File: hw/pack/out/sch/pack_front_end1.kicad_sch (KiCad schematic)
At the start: 14 parts, among them J1 3.5mm locking, U3 OPA1656

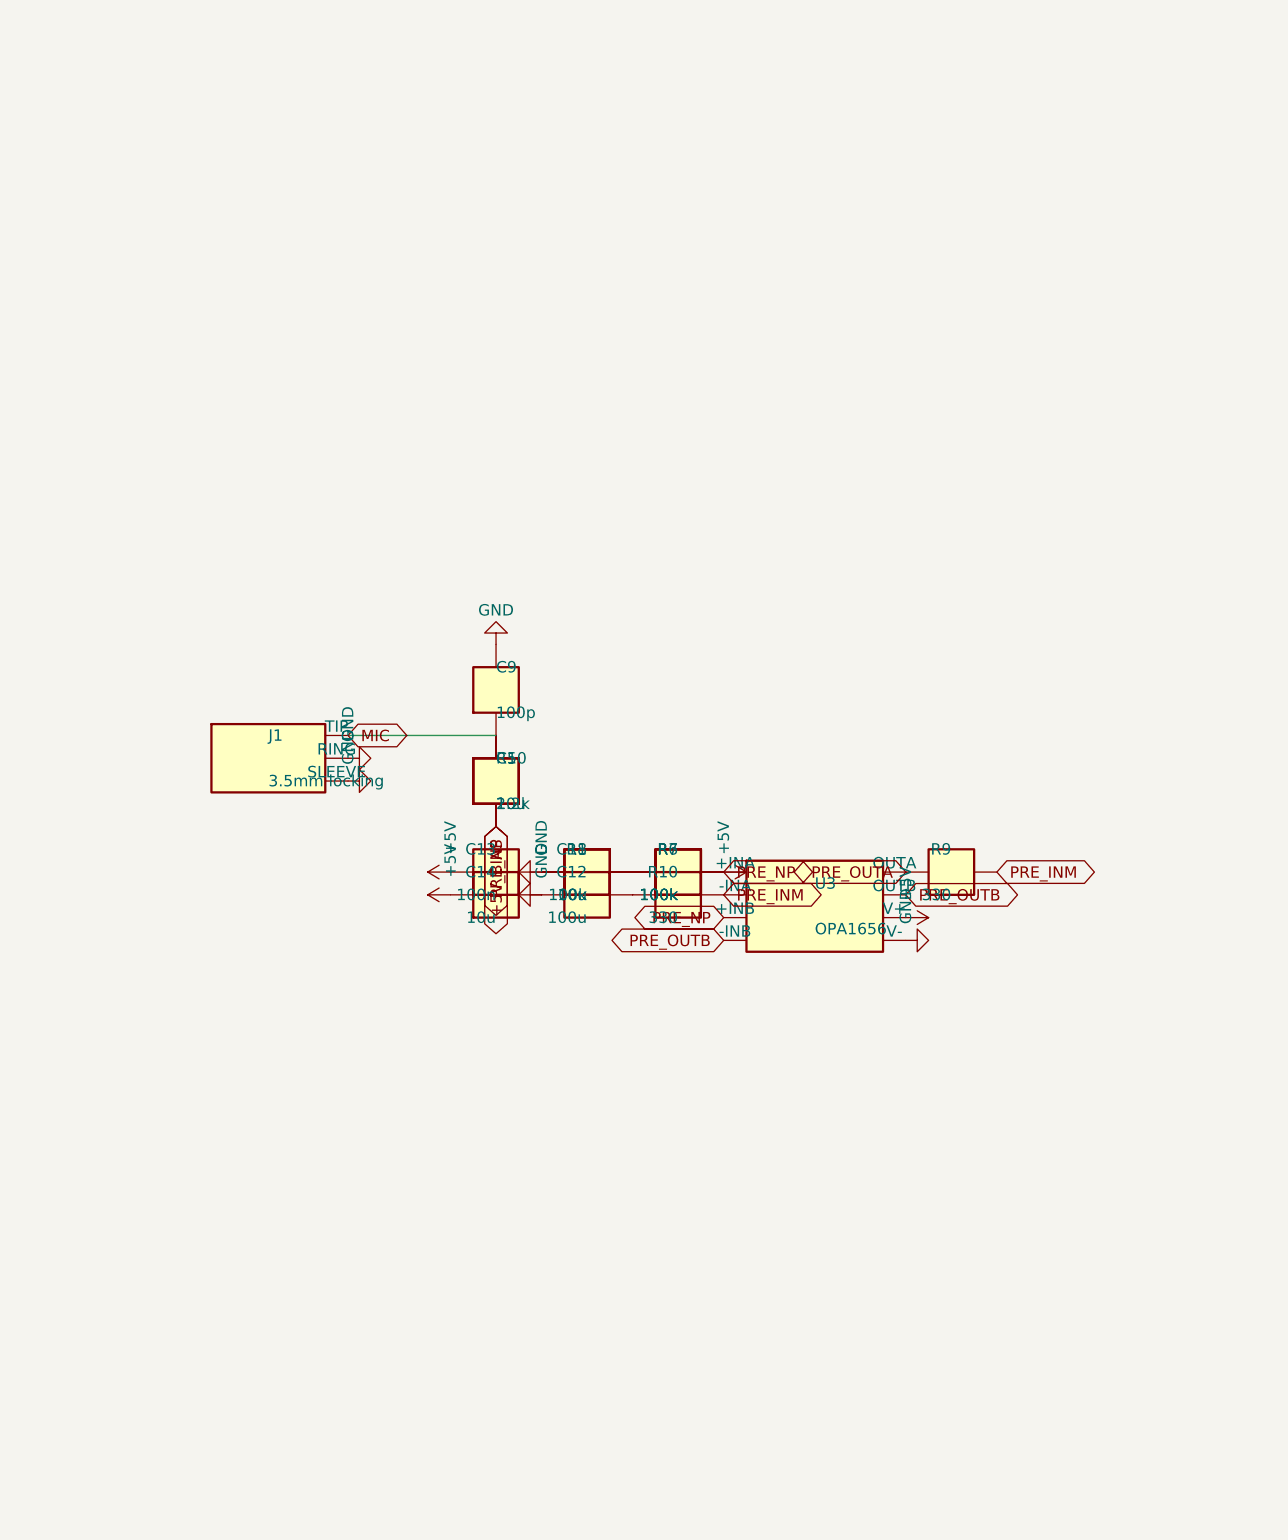
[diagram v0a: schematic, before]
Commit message: hw/pack: review fixes for #75 (op-amp CM, hot-plug protection, CI, cutoff, LEDs) (#31)
- VCM 180k/100k (1.77 V) keeps OPA1656 +IN inside V+ - 2.25 V; SPICE clamp 0.25/4.70 V,
  test asserts input CM, ADC pin (1.375 V) and prints numbers in CI (-rP)
- tip ESD (TPD1E10B06), BAV199 clamp + 100R ahead of the op-amp; C9 22p; noise 0.96 uV
- CI installs skidl==3.0.0, pack test fails (not skips) under CI, stale-output diff check
- no PTC; cell sensed at BAT+; firmware cutoff 3.2 V derived in audit.py; PK-8 LED
  thresholds -10/-7 dBFS; real LED MPNs; VDDH decoupling; audit prints DK-price BOM

Co-Authored-By: Claude Opus 5.5 <noreply@anthropic.com>
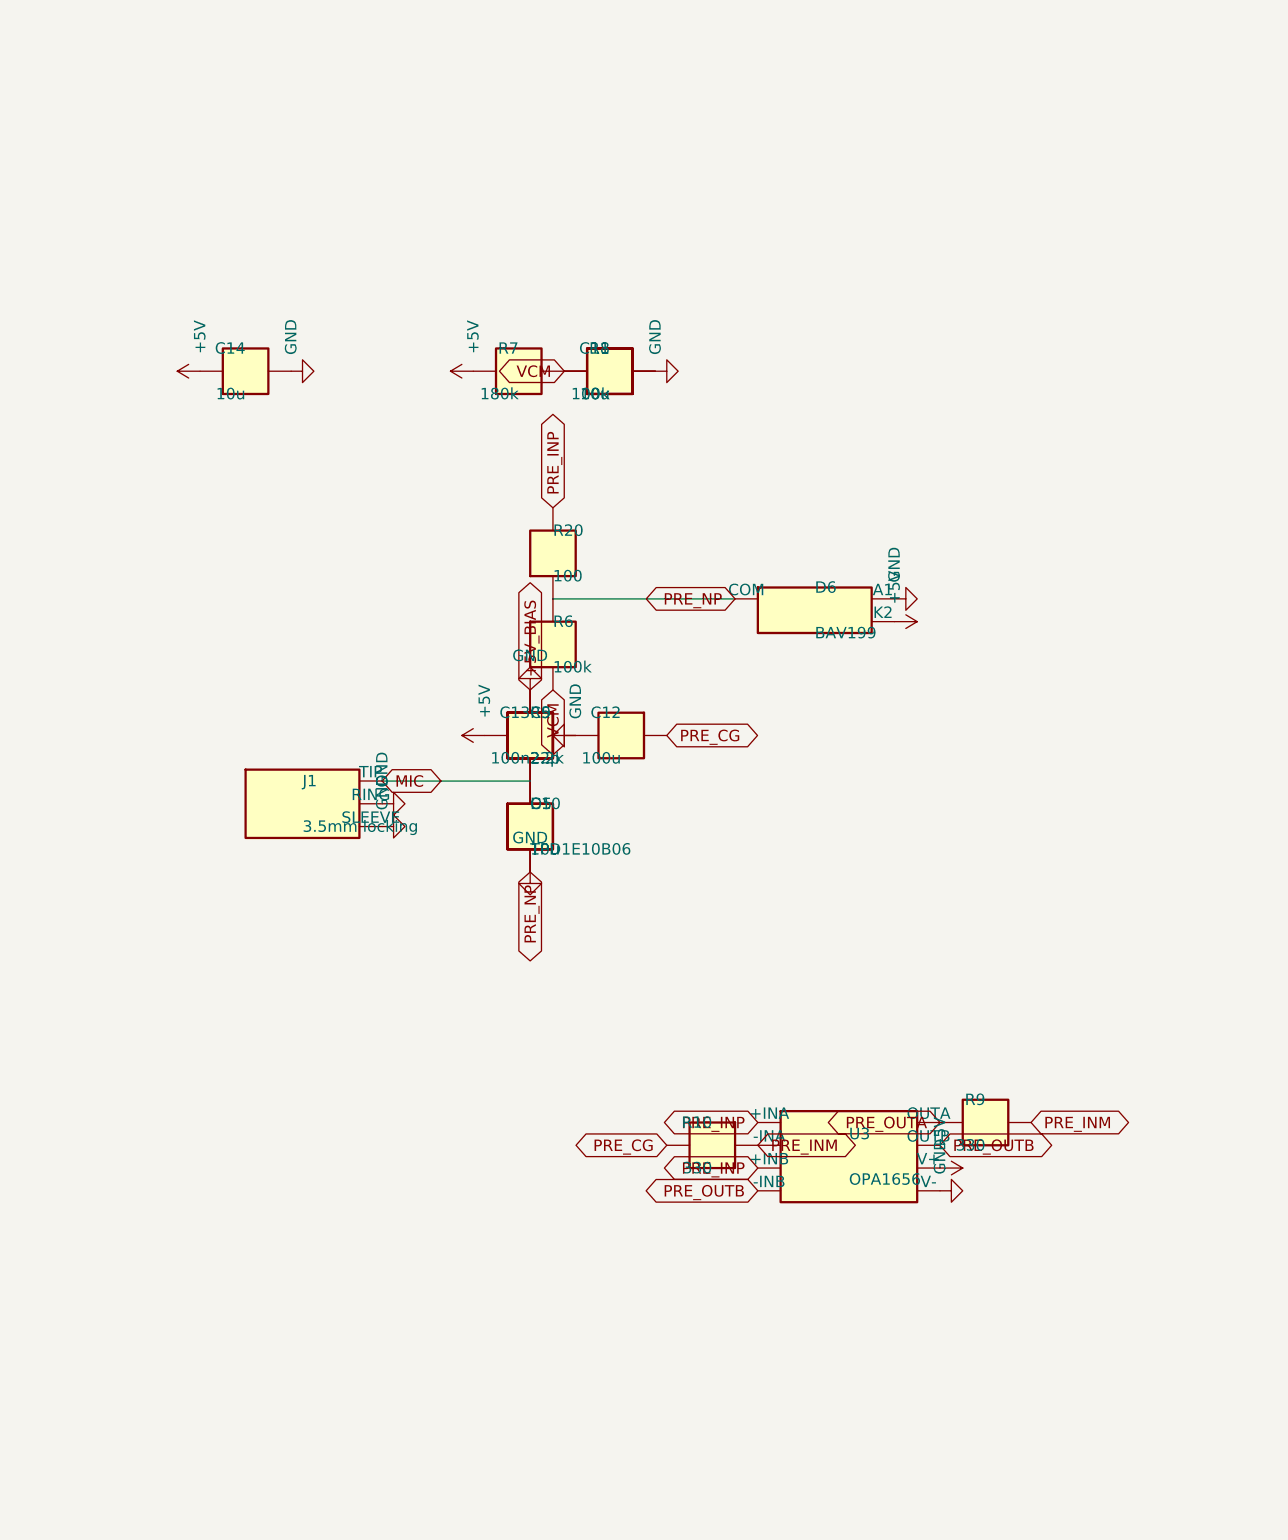
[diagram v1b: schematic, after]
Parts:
- added D5: TPD1E10B06, Diode_SMD:D_0402_1005Metric, symbol openpack:ESD_Bidir
- added D6: BAV199, Package_TO_SOT_SMD:SOT-23, symbol openpack:BAV199
- added R20: 100, Resistor_SMD:R_0402_1005Metric, symbol openpack:R
- C9: value 100p -> 22p; MPN C_100p_0402_C0G -> C_22p_0402_C0G
- R7: value 100k -> 180k
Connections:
- net +5V: now also D6.2 (K2); no longer C10.2, R5.1, R6.1, U3.3 (+INA), U3.5 (+INB)
- net GND: now also C10.2, R5.1, R6.1, D5.2, D6.1 (A1), D6.3 (COM), R20.1
- net MIC: now also D5.1
- net VCM: now reaches C11.1, R6.2, R7.2, R8.1
- net PRE_CG: now reaches C12.1, R10.2
- new net PRE_INP: R20.2, U3.3 (+INA), U3.5 (+INB)
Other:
- moved on the sheet: C10, C11, C12, C13, C14, C9, J1, R10, R5, R6, R7, R8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

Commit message: hw/pack: 3 A chip fuse (23 mOhm) on BAT+, cutoff re-derived, BOM $34.98 (#31)
Co-Authored-By: Claude Opus 5.5 <noreply@anthropic.com>
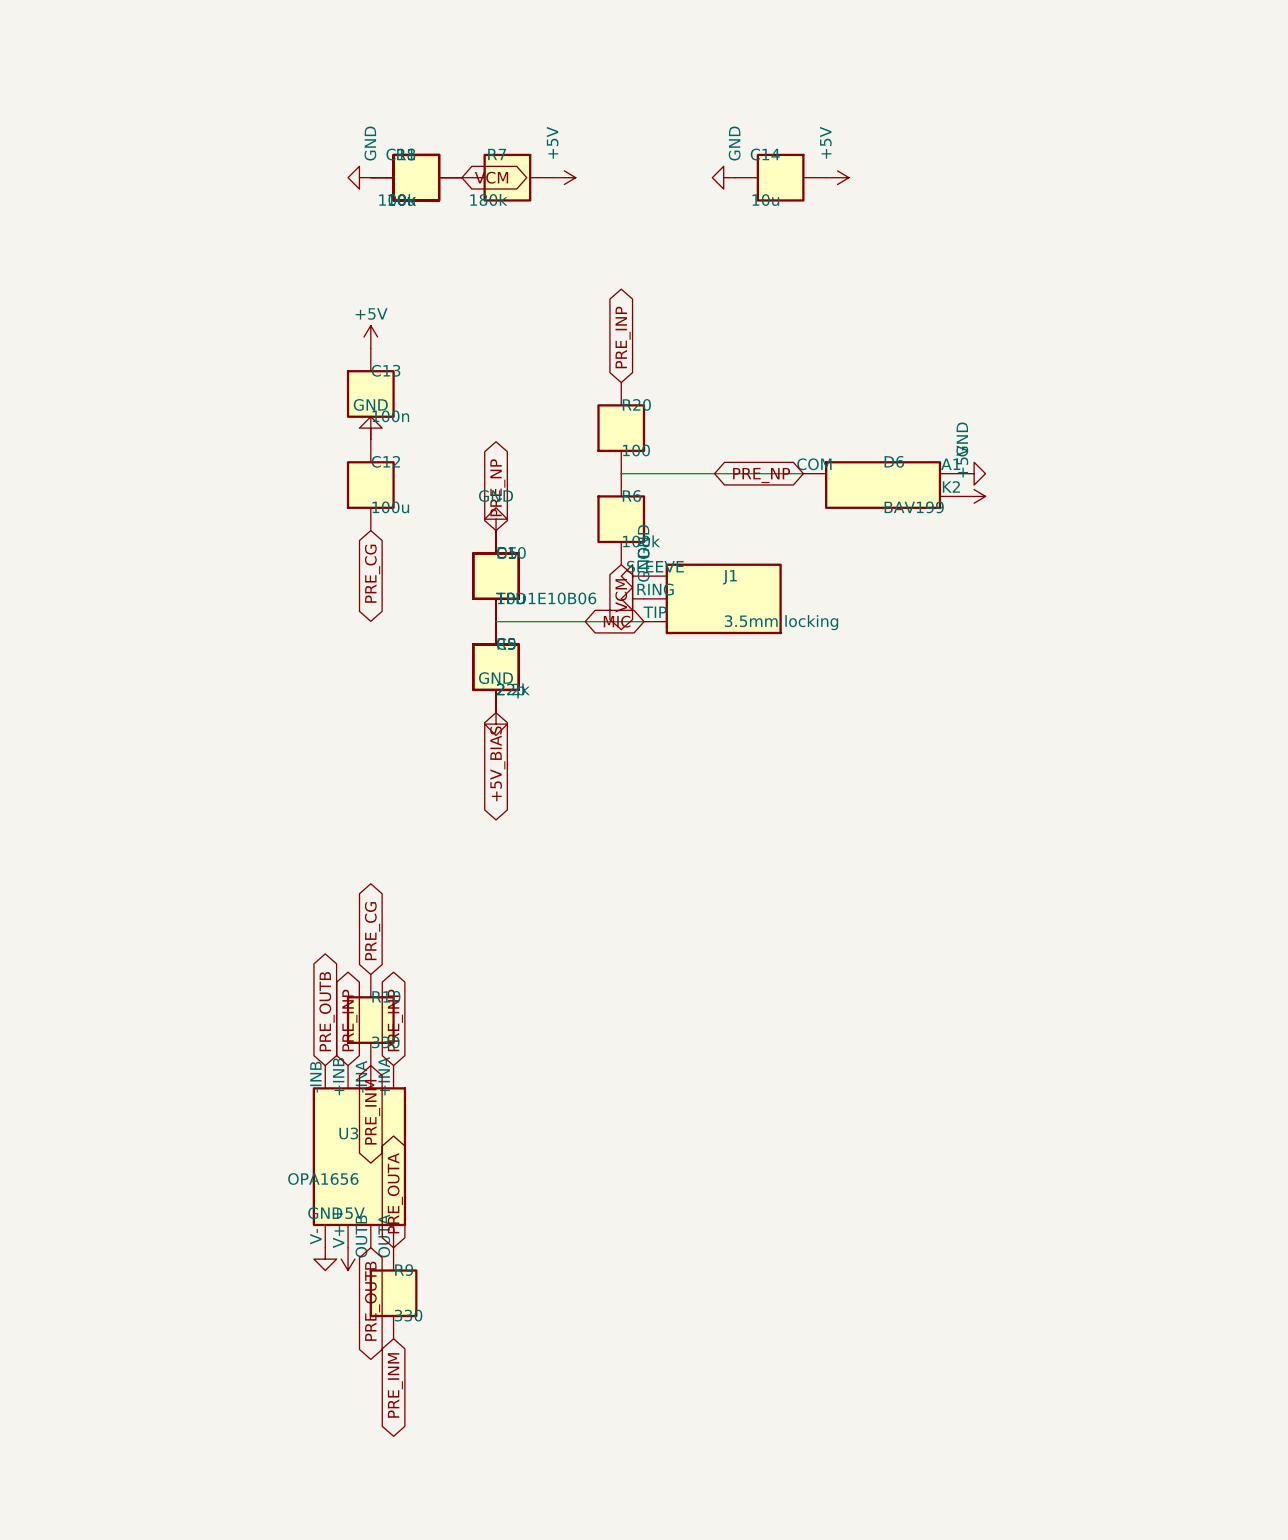
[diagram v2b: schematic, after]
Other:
- moved on the sheet: C10, C11, C12, C13, C14, C9, D5, D6, J1, R10, R20, R5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

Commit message: pack: restore battery-sense divider (R13/C30) (#84)
* hw/pack: restore battery-sense divider R13/C30 hidden in a comment

Co-Authored-By: Claude Sonnet 5.5 <noreply@anthropic.com>

* tests: cite nRF5340 SAADC pin limit (VDD) from the product spec

Co-Authored-By: Claude Sonnet 5.5 <noreply@anthropic.com>

* hw/pack: price 0402 resistors and 100n caps from LCSC qty-100 pages; UK BOM refs; merge main

Co-Authored-By: Claude Sonnet 5.5 <noreply@anthropic.com>

---------

Co-authored-by: Claude Sonnet 5.5 <noreply@anthropic.com>
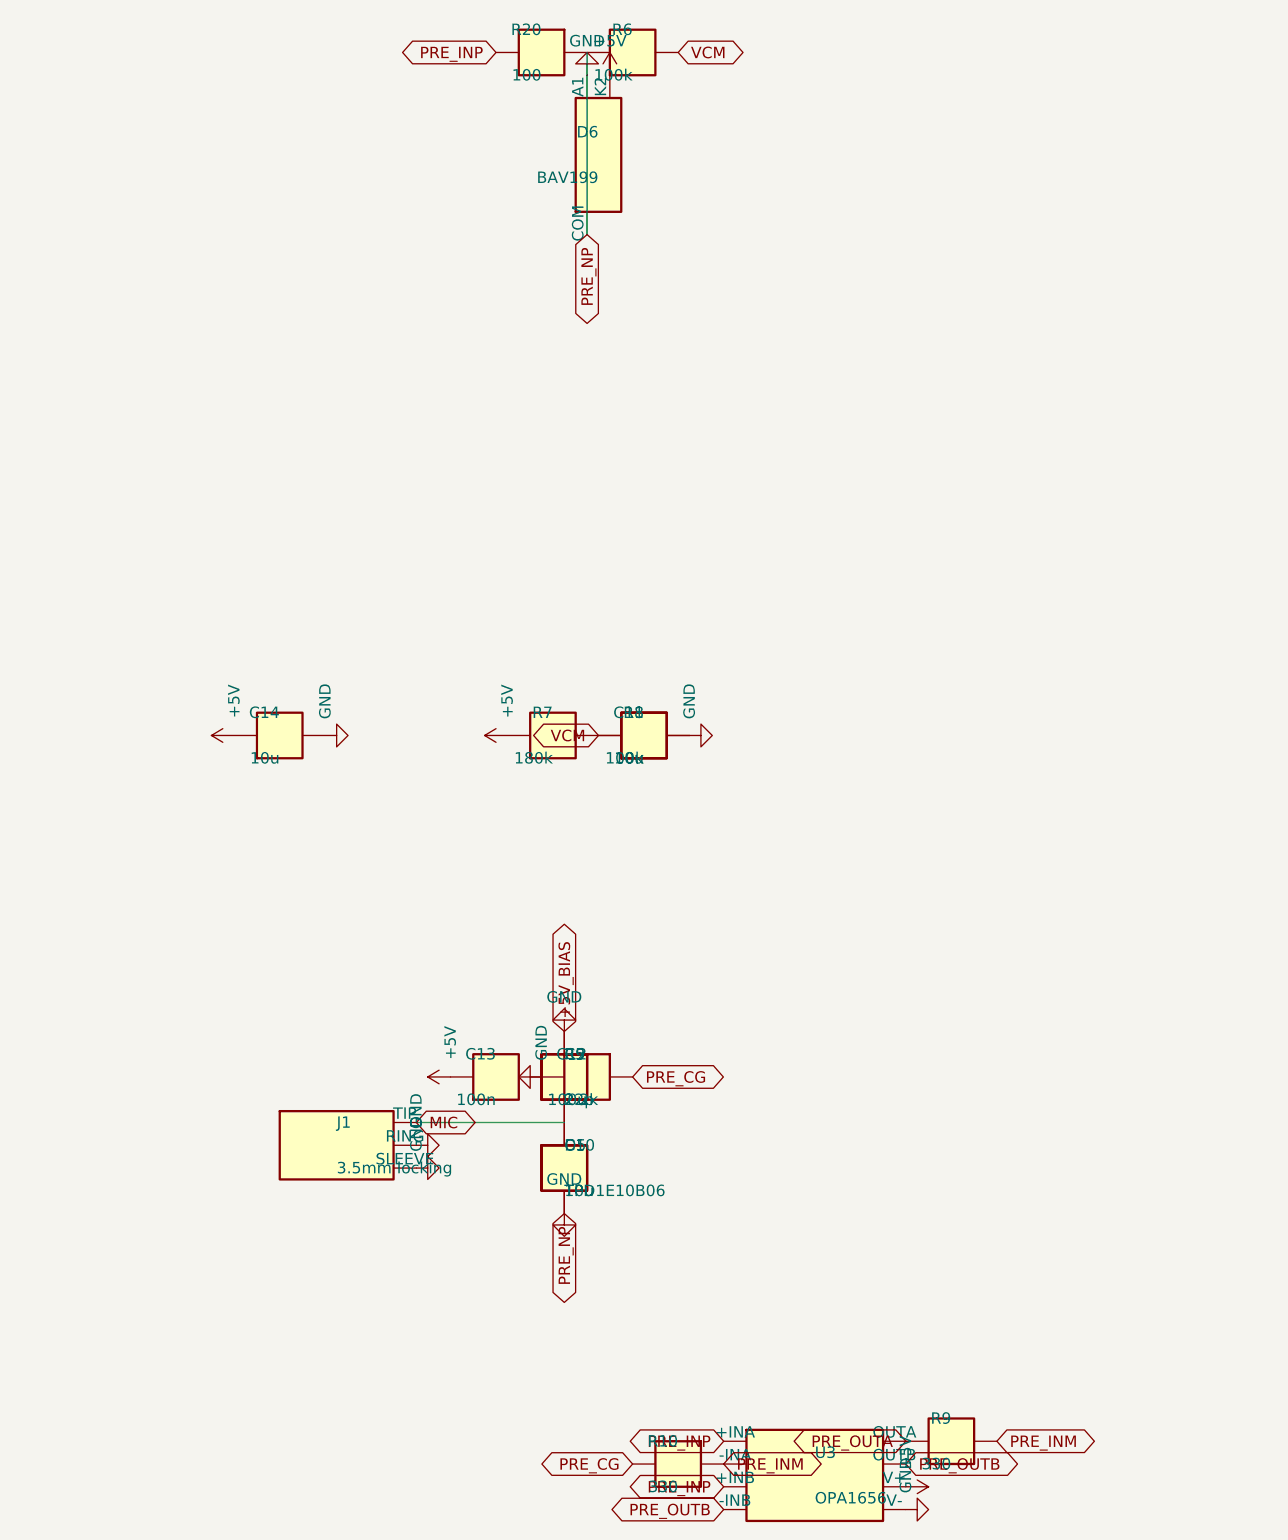
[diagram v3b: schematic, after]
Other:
- moved on the sheet: C10, C11, C12, C13, C14, C9, D5, D6, J1, R10, R20, R5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
